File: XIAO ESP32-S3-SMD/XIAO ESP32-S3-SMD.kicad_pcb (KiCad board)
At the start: 2 copper layers, 34.6 x 37.9 mm, 15 parts, among them U2 XIAO-ESP32-S3-SMD

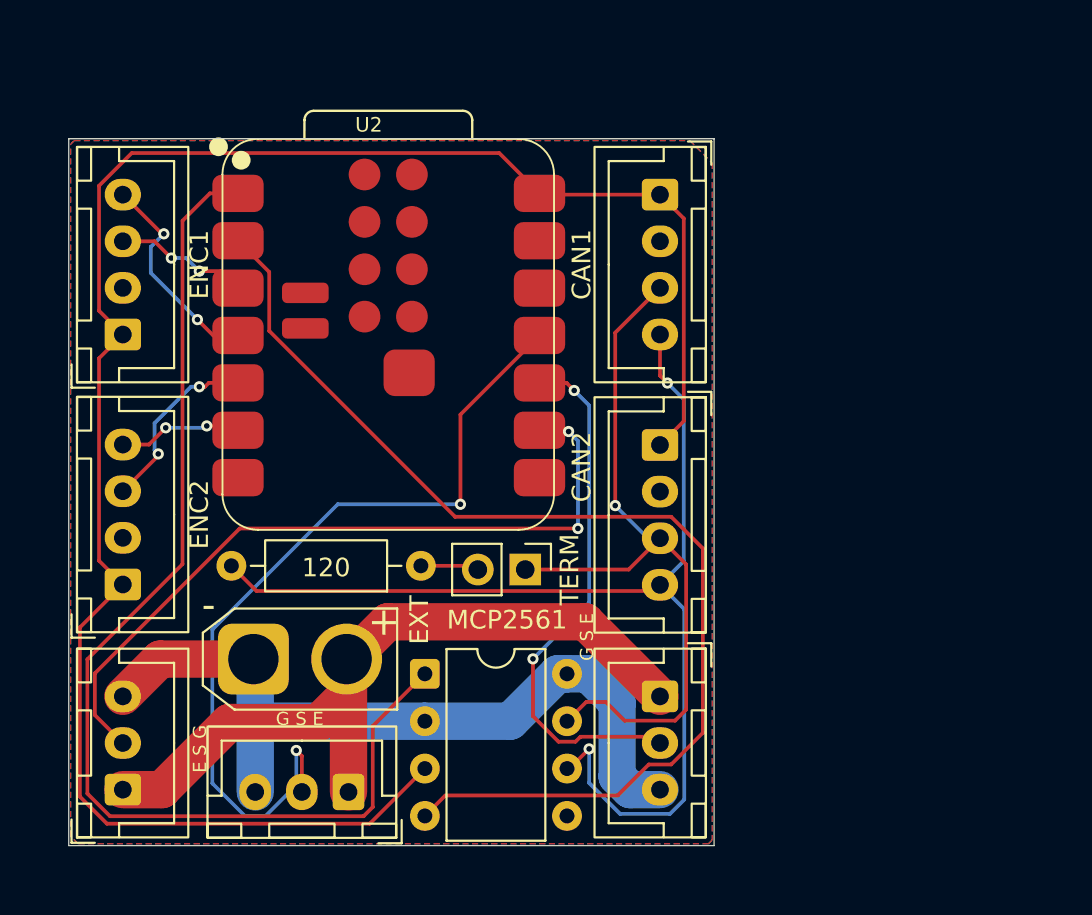
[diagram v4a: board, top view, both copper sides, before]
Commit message: 製造データ出力
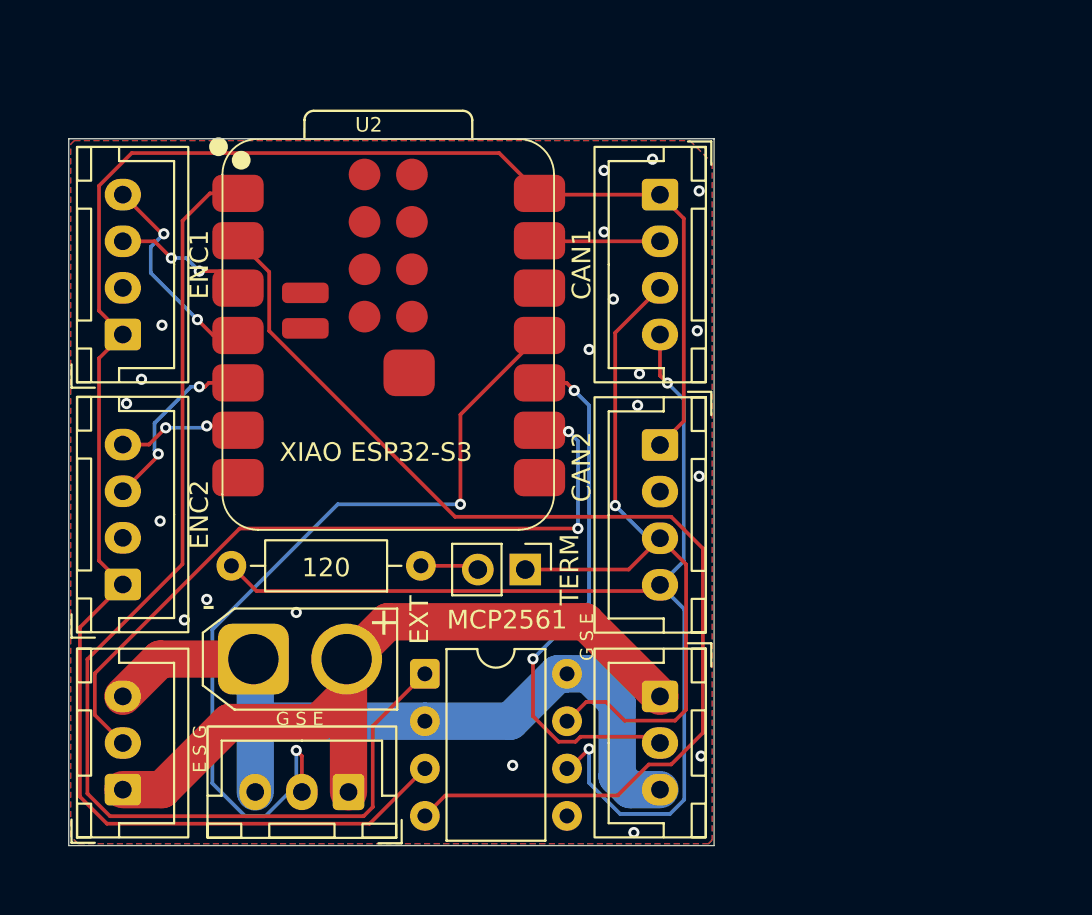
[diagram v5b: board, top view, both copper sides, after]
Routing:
- net GND: track 42.6 -> 49.1 mm, vias 0 -> 20
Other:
- board text added: "XIAO ESP32-S3"
- board text added: "XIAO ESP32-S3 can2io v1.0"
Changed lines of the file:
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@@
+		)
+	)
+	(gr_text "XIAO ESP32-S3"
+		(at 144 79.79625 0)
+		(layer "F.SilkS")
+		(effects
+			(font
+				(size 1 1)
+				(thickness 0.1)
+			)
+			(justify left bottom)
 		)
 	)
@@
 		)
 	)
+	(gr_text "XIAO ESP32-S3\ncan2io v1.0"
+		(at 157 87.5 90)
+		(layer "B.SilkS" knockout)
+		(effects
+			(font
+				(size 1 1)
+				(thickness 0.2)
+				(bold yes)
+				(italic yes)
+			)
+			(justify left bottom mirror)
+		)
+	)
 	(segment
 		(start 148.509744 98.725)
@@
 		(layer "F.Cu")
 		(net "CAN_TX")
+	)
+	(segment
+		(start 164.4 67.9)
+		(end 157.968 67.9)
+		(width 0.2)
+		(layer "F.Cu")
+		(net "GND")
 	)
 	(segment
@@
 		(net "GND")
 	)
+	(segment
+		(start 157.968 67.9)
+		(end 157.94 67.872)
+		(width 0.2)
+		(layer "F.Cu")
+		(net "GND")
+	)
+	(via
+		(at 137.6 82.9)
+		(size 0.6)
+		(drill 0.3)
+		(layers "F.Cu" "B.Cu")
+		(free yes)
+		(net "GND")
+	)
+	(via
+		(at 163.2 76.7)
+		(size 0.6)
+		(drill 0.3)
+		(layers "F.Cu" "B.Cu")
+		(free yes)
+		(net "GND")
+	)
+	(via
+		(at 138.9 88.2)
+		(size 0.6)
+		(drill 0.3)
+		(layers "F.Cu" "B.Cu")
+		(free yes)
+		(net "GND")
+	)
+	(via
+		(at 144.9 87.8)
+		(size 0.6)
+		(drill 0.3)
+		(layers "F.Cu" "B.Cu")
+		(free yes)
+		(net "GND")
+	)
+	(via
+		(at 166.5 65.2)
+		(size 0.6)
+		(drill 0.3)
+		(layers "F.Cu" "B.Cu")
+		(free yes)
+		(net "GND")
+	)
+	(via
+		(at 161.4 64.1)
+		(size 0.6)
+		(drill 0.3)
+		(layers "F.Cu" "B.Cu")
+		(free yes)
+		(net "GND")
+	)
+	(via
+		(at 137.7 72.4)
+		(size 0.6)
+		(drill 0.3)
+		(layers "F.Cu" "B.Cu")
+		(free yes)
+		(net "GND")
+	)
+	(via
+		(at 161.4 67.4)
+		(size 0.6)
+		(drill 0.3)
+		(layers "F.Cu" "B.Cu")
+		(free yes)
+		(net "GND")
+	)
+	(via
+		(at 164 63.5)
+		(size 0.6)
+		(drill 0.3)
+		(layers "F.Cu" "B.Cu")
+		(free yes)
+		(net "GND")
+	)
+	(via
+		(at 166.6 95.5)
+		(size 0.6)
+		(drill 0.3)
+		(layers "F.Cu" "B.Cu")
+		(free yes)
+		(net "GND")
+	)
+	(via
+		(at 166.5 80.5)
+		(size 0.6)
+		(drill 0.3)
+		(layers "F.Cu" "B.Cu")
+		(free yes)
+		(net "GND")
+	)
+	(via
+		(at 166.4 72.7)
+		(size 0.6)
+		(drill 0.3)
+		(layers "F.Cu" "B.Cu")
+		(free yes)
+		(net "GND")
+	)
+	(via
+		(at 163.3 75)
+		(size 0.6)
+		(drill 0.3)
+		(layers "F.Cu" "B.Cu")
+		(free yes)
+		(net "GND")
+	)
+	(via
+		(at 156.5 96)
+		(size 0.6)
+		(drill 0.3)
+		(layers "F.Cu" "B.Cu")
+		(free yes)
+		(net "GND")
+	)
+	(via
+		(at 160.6 73.7)
+		(size 0.6)
+		(drill 0.3)
+		(layers "F.Cu" "B.Cu")
+		(free yes)
+		(net "GND")
+	)
+	(via
+		(at 163 99.6)
+		(size 0.6)
+		(drill 0.3)
+		(layers "F.Cu" "B.Cu")
+		(free yes)
+		(net "GND")
+	)
+	(via
+		(at 140.1 87.1)
+		(size 0.6)
+		(drill 0.3)
+		(layers "F.Cu" "B.Cu")
+		(free yes)
+		(net "GND")
+	)
+	(via
+		(at 135.8 76.6)
+		(size 0.6)
+		(drill 0.3)
+		(layers "F.Cu" "B.Cu")
+		(free yes)
+		(net "GND")
+	)
+	(via
+		(at 161.9 71)
+		(size 0.6)
+		(drill 0.3)
+		(layers "F.Cu" "B.Cu")
+		(free yes)
+		(net "GND")
+	)
+	(via
+		(at 136.6 75.3)
+		(size 0.6)
+		(drill 0.3)
+		(layers "F.Cu" "B.Cu")
+		(free yes)
+		(net "GND")
+	)
